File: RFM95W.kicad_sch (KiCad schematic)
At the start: 3 parts, among them U2 RFM95W-915S2

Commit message: ongoing
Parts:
- R35: footprint ProjectLib:R_0603_1608Metric -> ProjectLib:R_0402_1005Metric
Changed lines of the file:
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@@
 			)
 		)
-		(property "Footprint" "ProjectLib:R_0603_1608Metric"
+		(property "Footprint" "ProjectLib:R_0402_1005Metric"
 			(at 96.266 81.534 90)
 			(effects

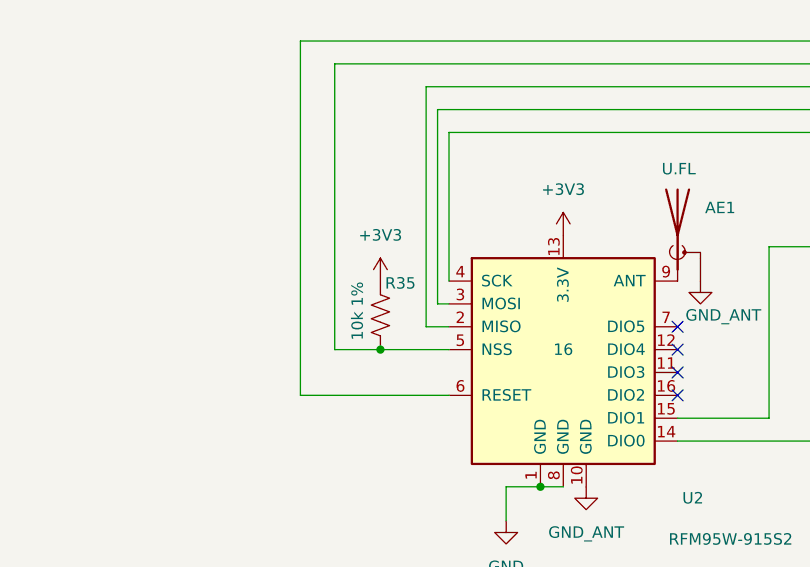
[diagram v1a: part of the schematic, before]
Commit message: adding MCU, ongoing.
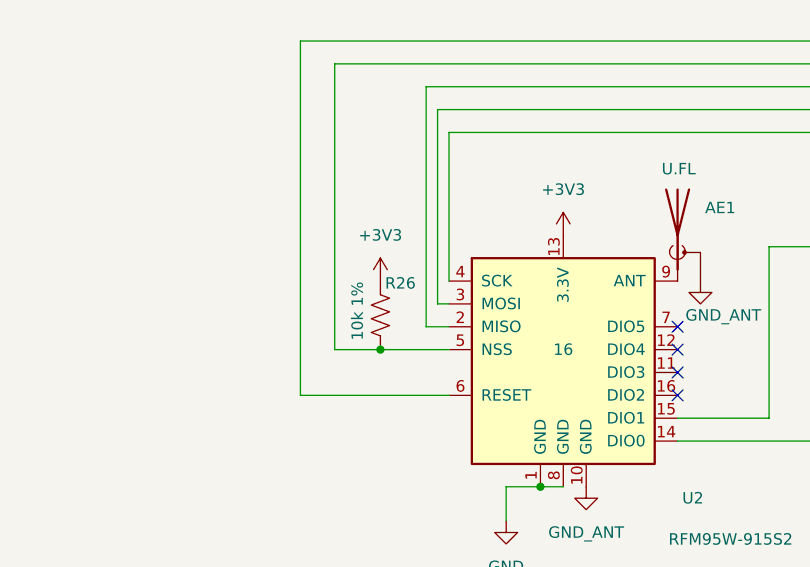
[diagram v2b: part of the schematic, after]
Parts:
- renumbered R35 to R26
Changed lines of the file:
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@@
 		(on_board yes)
 		(dnp no)
-		(property "Reference" "R35"
+		(property "Reference" "R26"
 			(at 95.758 77.724 0)
 			(effects
@@
 			(project "multiplexI2C"
 				(path "/0c2d0c14-8850-4a30-bb78-b2f40cb442ba/8bb5a1a1-4d5b-4032-b28f-cb44ec0cd683"
-					(reference "R35")
+					(reference "R26")
 					(unit 1)
 				)
@@
 		(dnp no)
 		(fields_autoplaced yes)
-		(property "Reference" "#PWR0104"
+		(property "Reference" "#PWR044"
 			(at 118.11 106.68 0)
 			(effects
@@
 			(project "multiplexI2C"
 				(path "/0c2d0c14-8850-4a30-bb78-b2f40cb442ba/8bb5a1a1-4d5b-4032-b28f-cb44ec0cd683"
-					(reference "#PWR0104")
+					(reference "#PWR044")
 					(unit 1)
 				)
@@
 		(on_board yes)
 		(dnp no)
-		(property "Reference" "#PWR0105"
+		(property "Reference" "#PWR045"
 			(at 130.81 83.82 0)
 			(effects
@@
 			(project "multiplexI2C"
 				(path "/0c2d0c14-8850-4a30-bb78-b2f40cb442ba/8bb5a1a1-4d5b-4032-b28f-cb44ec0cd683"
-					(reference "#PWR0105")
+					(reference "#PWR045")
 					(unit 1)
 				)
@@
 		(dnp no)
 		(fields_autoplaced yes)
-		(property "Reference" "#PWR0102"
+		(property "Reference" "#PWR041"
 			(at 95.25 81.28 0)
 			(effects
@@
 			(project "multiplexI2C"
 				(path "/0c2d0c14-8850-4a30-bb78-b2f40cb442ba/8bb5a1a1-4d5b-4032-b28f-cb44ec0cd683"
-					(reference "#PWR0102")
+					(reference "#PWR041")
 					(unit 1)
 				)
@@
 		(dnp no)
 		(fields_autoplaced yes)
-		(property "Reference" "#PWR0101"
+		(property "Reference" "#PWR042"
 			(at 109.22 110.49 0)
 			(effects
@@
 			(project "multiplexI2C"
 				(path "/0c2d0c14-8850-4a30-bb78-b2f40cb442ba/8bb5a1a1-4d5b-4032-b28f-cb44ec0cd683"
-					(reference "#PWR0101")
+					(reference "#PWR042")
 					(unit 1)
 				)
@@
 		(dnp no)
 		(fields_autoplaced yes)
-		(property "Reference" "#PWR0103"
+		(property "Reference" "#PWR043"
 			(at 115.57 76.2 0)
 			(effects
@@
 			(project "multiplexI2C"
 				(path "/0c2d0c14-8850-4a30-bb78-b2f40cb442ba/8bb5a1a1-4d5b-4032-b28f-cb44ec0cd683"
-					(reference "#PWR0103")
-					(unit 1)
-				)
+					(reference "#PWR043")
+					(unit 1)
+				)

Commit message: ongoing.
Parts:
- AE1: MfgPart U.FL-R-SMT-1 -> U.FL-R-SMT-K(800)
- renumbered R26 to R28, U2 to U7
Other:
- title: Multiplex I2C to Screw Terminal connectors -> RFM95W 915MHz
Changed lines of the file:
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@@
 	(paper "A4")
 	(title_block
-		(title "Multiplex I2C to Screw Terminal connectors")
-		(date "2025-09-07")
-		(rev "v0.2.0")
+		(title "RFM95W 915MHz")
+		(date "2025-09-15")
+		(rev "v0.2.2")
 	)
 	(bus_alias "SPI"
@@
 		(on_board yes)
 		(dnp no)
-		(property "Reference" "R26"
+		(property "Reference" "R28"
 			(at 95.758 77.724 0)
 			(effects
@@
 			)
 		)
-		(property "Datasheet" "~"
+		(property "Datasheet" ""
 			(at 95.25 81.28 0)
 			(effects
@@
 		)
 		(instances
-			(project "multiplexI2C"
-				(path "/0c2d0c14-8850-4a30-bb78-b2f40cb442ba/8bb5a1a1-4d5b-4032-b28f-cb44ec0cd683"
-					(reference "R26")
+			(project ""
+				(path "/0c2d0c14-8850-4a30-bb78-b2f40cb442ba/2810e5bd-88e3-445e-9497-ea39bfab4c18/e20fbd44-1da9-4c99-bcb2-270c25737e1b"
+					(reference "R28")
 					(unit 1)
 				)
@@
 		(dnp no)
 		(fields_autoplaced yes)
-		(property "Reference" "#PWR044"
+		(property "Reference" "#PWR066"
 			(at 118.11 106.68 0)
 			(effects
@@
 		)
 		(instances
-			(project "multiplexI2C"
-				(path "/0c2d0c14-8850-4a30-bb78-b2f40cb442ba/8bb5a1a1-4d5b-4032-b28f-cb44ec0cd683"
-					(reference "#PWR044")
+			(project ""
+				(path "/0c2d0c14-8850-4a30-bb78-b2f40cb442ba/2810e5bd-88e3-445e-9497-ea39bfab4c18/e20fbd44-1da9-4c99-bcb2-270c25737e1b"
+					(reference "#PWR066")
 					(unit 1)
 				)
@@
 		(on_board yes)
 		(dnp no)
-		(property "Reference" "#PWR045"
+		(property "Reference" "#PWR065"
 			(at 130.81 83.82 0)
 			(effects
@@
 		)
 		(instances
-			(project "multiplexI2C"
-				(path "/0c2d0c14-8850-4a30-bb78-b2f40cb442ba/8bb5a1a1-4d5b-4032-b28f-cb44ec0cd683"
-					(reference "#PWR045")
+			(project ""
+				(path "/0c2d0c14-8850-4a30-bb78-b2f40cb442ba/2810e5bd-88e3-445e-9497-ea39bfab4c18/e20fbd44-1da9-4c99-bcb2-270c25737e1b"
+					(reference "#PWR065")
 					(unit 1)
 				)
@@
 		(dnp no)
 		(fields_autoplaced yes)
-		(property "Reference" "#PWR041"
+		(property "Reference" "#PWR0102"
 			(at 95.25 81.28 0)
 			(effects
@@
 		)
 		(instances
-			(project "multiplexI2C"
-				(path "/0c2d0c14-8850-4a30-bb78-b2f40cb442ba/8bb5a1a1-4d5b-4032-b28f-cb44ec0cd683"
-					(reference "#PWR041")
+			(project "SensorProject_t16-pcb"
+				(path "/0c2d0c14-8850-4a30-bb78-b2f40cb442ba/2810e5bd-88e3-445e-9497-ea39bfab4c18/e20fbd44-1da9-4c99-bcb2-270c25737e1b"
+					(reference "#PWR0102")
 					(unit 1)
 				)
@@
 		(dnp no)
 		(fields_autoplaced yes)
-		(property "Reference" "#PWR042"
+		(property "Reference" "#PWR0103"
 			(at 109.22 110.49 0)
 			(effects
@@
 		)
 		(instances
-			(project "multiplexI2C"
-				(path "/0c2d0c14-8850-4a30-bb78-b2f40cb442ba/8bb5a1a1-4d5b-4032-b28f-cb44ec0cd683"
-					(reference "#PWR042")
+			(project "SensorProject_t16-pcb"
+				(path "/0c2d0c14-8850-4a30-bb78-b2f40cb442ba/2810e5bd-88e3-445e-9497-ea39bfab4c18/e20fbd44-1da9-4c99-bcb2-270c25737e1b"
+					(reference "#PWR0103")
 					(unit 1)
 				)
@@
 		(dnp no)
 		(fields_autoplaced yes)
-		(property "Reference" "#PWR043"
+		(property "Reference" "#PWR0101"
 			(at 115.57 76.2 0)
 			(effects
@@
 		)
 		(instances
-			(project "multiplexI2C"
-				(path "/0c2d0c14-8850-4a30-bb78-b2f40cb442ba/8bb5a1a1-4d5b-4032-b28f-cb44ec0cd683"
-					(reference "#PWR043")
+			(project "SensorProject_t16-pcb"
+				(path "/0c2d0c14-8850-4a30-bb78-b2f40cb442ba/2810e5bd-88e3-445e-9497-ea39bfab4c18/e20fbd44-1da9-4c99-bcb2-270c25737e1b"
+					(reference "#PWR0101")
 					(unit 1)
 				)
@@
 		(on_board yes)
 		(dnp no)
-		(property "Reference" "U2"
+		(property "Reference" "U7"
 			(at 128.778 101.6 0)
 			(effects
@@
 			)
 		)
-		(property "Datasheet" "https://www.hoperf.com/modules/lora/RFM95W.html"
+		(property "Datasheet" "https://cdn.sparkfun.com/assets/learn_tutorials/8/0/4/RFM95_96_97_98W.pdf"
 			(at 31.75 43.18 0)
 			(effects
@@
 			)
 		)
-		(property "Description" "LoRa module, SPI, 915MHz, spreading factor 6 to12, bandwidth 125 to 500kHz, -111 to -136 dBm, SMD-16"
+		(property "Description" "LoRa module, SPI, 915 MHz,  SMD-16"
 			(at 115.57 85.09 0)
 			(effects
@@
 		)
 		(instances
-			(project "multiplexI2C"
-				(path "/0c2d0c14-8850-4a30-bb78-b2f40cb442ba/8bb5a1a1-4d5b-4032-b28f-cb44ec0cd683"
-					(reference "U2")
+			(project "SensorProject_t16-pcb"
+				(path "/0c2d0c14-8850-4a30-bb78-b2f40cb442ba/2810e5bd-88e3-445e-9497-ea39bfab4c18/e20fbd44-1da9-4c99-bcb2-270c25737e1b"
+					(reference "U7")
 					(unit 1)
 				)
@@
 			)
 		)
-		(property "Datasheet" "~"
+		(property "Datasheet" "https://www.hirose.com/en/product/p/CL0480-0761-0-00"
 			(at 128.27 69.85 0)
 			(effects
@@
 			)
 		)
-		(property "Description" "Antenna with extra pin for shielding"
+		(property "Description" "Antenna connector with shielding"
 			(at 128.27 72.39 0)
 			(effects
@@
 			)
 		)
-		(property "MfgPart" "U.FL-R-SMT-1"
+		(property "MfgPart" "U.FL-R-SMT-K(800)"
 			(at 128.27 72.39 0)
 			(effects
@@
 		)
 		(instances
-			(project "multiplexI2C"
-				(path "/0c2d0c14-8850-4a30-bb78-b2f40cb442ba/8bb5a1a1-4d5b-4032-b28f-cb44ec0cd683"
+			(project ""
+				(path "/0c2d0c14-8850-4a30-bb78-b2f40cb442ba/2810e5bd-88e3-445e-9497-ea39bfab4c18/e20fbd44-1da9-4c99-bcb2-270c25737e1b"
 					(reference "AE1")
 					(unit 1)

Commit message: ERC and DRC good. Needs fab layer cleanup.
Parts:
- renumbered AE1 to AE701, R28 to R701, U7 to U701
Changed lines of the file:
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@@
 		(on_board yes)
 		(dnp no)
-		(property "Reference" "R28"
+		(property "Reference" "R701"
 			(at 95.758 77.724 0)
 			(effects
@@
 			(project ""
 				(path "/0c2d0c14-8850-4a30-bb78-b2f40cb442ba/2810e5bd-88e3-445e-9497-ea39bfab4c18/e20fbd44-1da9-4c99-bcb2-270c25737e1b"
-					(reference "R28")
+					(reference "R701")
 					(unit 1)
 				)
@@
 		(on_board yes)
 		(dnp no)
-		(property "Reference" "U7"
+		(property "Reference" "U701"
 			(at 128.778 101.6 0)
 			(effects
@@
 			(project "SensorProject_t16-pcb"
 				(path "/0c2d0c14-8850-4a30-bb78-b2f40cb442ba/2810e5bd-88e3-445e-9497-ea39bfab4c18/e20fbd44-1da9-4c99-bcb2-270c25737e1b"
-					(reference "U7")
+					(reference "U701")
 					(unit 1)
 				)
@@
 		(on_board yes)
 		(dnp no)
-		(property "Reference" "AE1"
+		(property "Reference" "AE701"
 			(at 131.318 69.342 0)
 			(effects
@@
 			(project ""
 				(path "/0c2d0c14-8850-4a30-bb78-b2f40cb442ba/2810e5bd-88e3-445e-9497-ea39bfab4c18/e20fbd44-1da9-4c99-bcb2-270c25737e1b"
-					(reference "AE1")
+					(reference "AE701")
 					(unit 1)
 				)
